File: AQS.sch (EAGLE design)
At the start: 44 parts, among them IC1 BME680, IC3 CP2102N-A01-GQFN24, IC4 ESPWROOM32, J1 ESP-PROG-2X3-1.27-SHROUDED, J2 M02X5-1.27-S, J3 USB-C-16P-16P, Q1 MMDT3904, Q2 2N7002

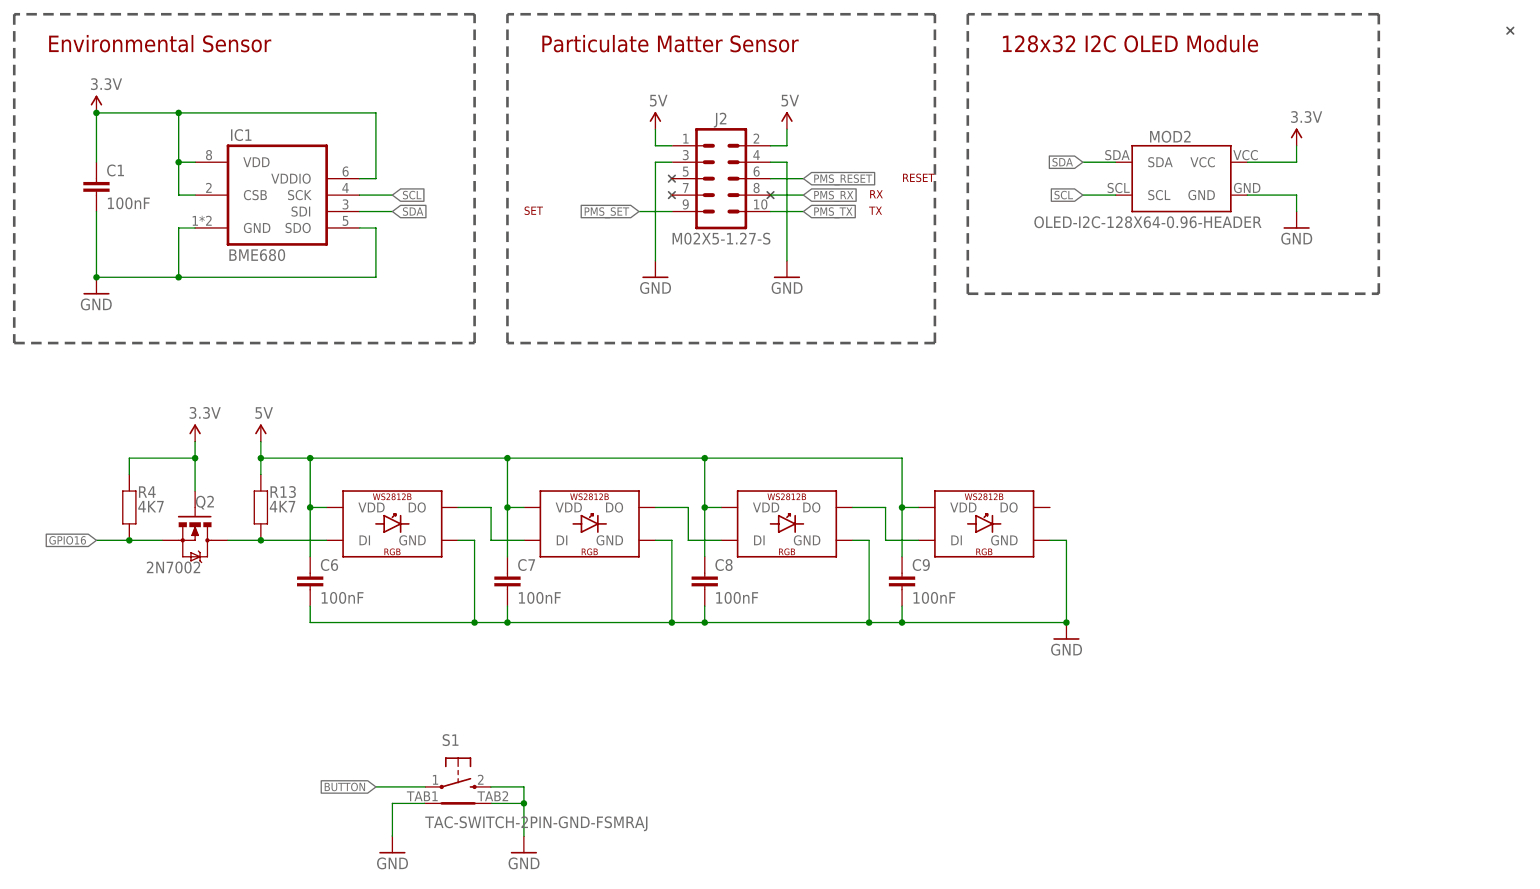
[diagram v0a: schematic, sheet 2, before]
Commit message: Major update to use 240x240 SPI LCD
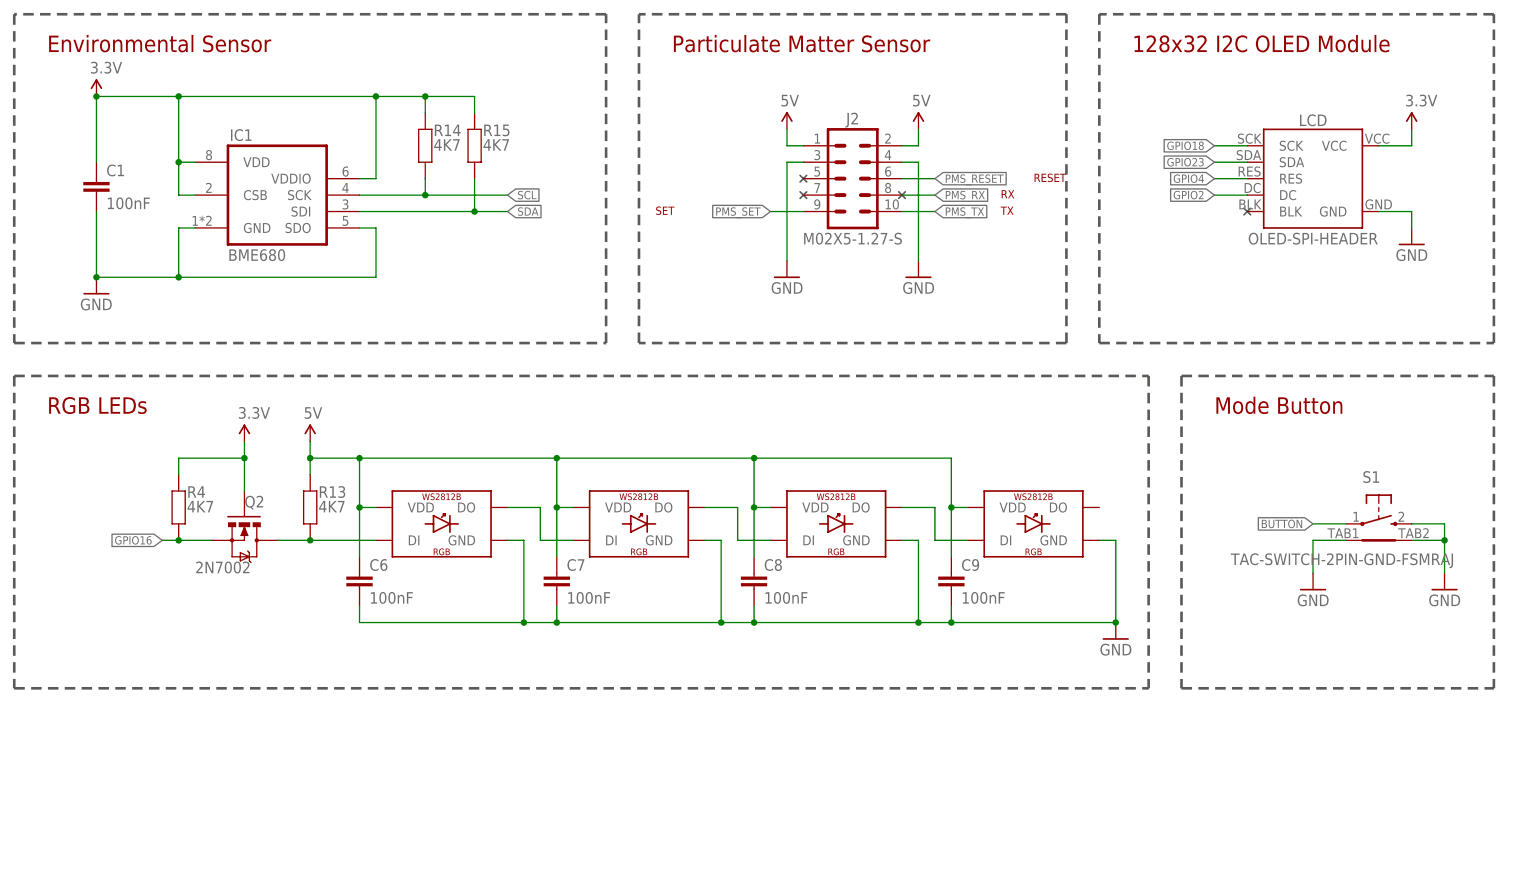
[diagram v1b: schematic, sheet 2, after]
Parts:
- removed MOD2: OLED-I2C-128X64-0.96-HEADER, SuperHouse-Displays:OLED-I2C-128X64-0.96-HEADER
- added LCD: OLED-SPI-HEADER, SuperHouse-Displays:OLED-SPI-HEADER
- added R14, R15: 4K7, SuperHouse-DiscreteSemi:RESISTOR0603
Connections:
- new net GPIO15: IC4.IO15
- new net GPIO18: IC4.IO18, LCD.SCK
- new net GPIO19: IC4.IO19
- new net GPIO2: IC4.IO2, LCD.DC
- new net GPIO23: IC4.IO23, LCD.SDA
- new net GPIO4: IC4.IO4, LCD.RES
- net 3.3V: now also LCD.VCC, R14.2, R15.2; no longer MOD2.VCC
- net GND: now also LCD.GND; no longer MOD2.GND
- net SCL: now also R14.1; no longer MOD2.SCL
- net SDA: now also R15.1; no longer MOD2.SDA
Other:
- note added: "Enable INPUT_PULLUP on IO35: button is active low"
- note added: "GPIO2: TFT_DC GPIO4: TFT_RST GPIO14: SET for PMS7003 GPIO15: TFT_CS GPIO16: WS2812B GPIO18: TFT_SCLK GPIO19: TFT_MISO GPIO23: TFT_MOSI GPIO25: SDA GPIO26: SCL GPIO34: Rx from PMS7003 Tx GPIO35: Button Firmware: https://github.com/openairproject/sensor-esp32"
- note added: "I2C Address: 0x77: BME680"
- note added: "Mode Button"
- note added: "RGB LEDs"
- note removed: "Assign pins Add ESPRog header and remove RST button? Remove power LED? Hide parts in bottom tab"
- note removed: "Enable INPUT_PULLUP on IO25, 26, 27: alert lines are active low"
- note removed: "GPIO14: SET for PMS7003 GPIO16: WS2812B GPIO25: SDA GPIO26: SCL GPIO34: Rx from PMS7003 Tx GPIO35: Button Firmware: https://github.com/openairproject/sensor-esp32"
- note removed: "I2C Addresses: 0x40: PCA9685 0x41: INA233 channel 1 0x42: INA233 channel 2 0x43: INA233 channel 3 0x66: ? 0x70: ? 0x77: BME280"
- note removed: "Power"
- moved on the sheet: C2, C3, C4, C5, C6, C7, C8, C9, IC4, J2, LED1, Q2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

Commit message: Moved mode button to GPIO0
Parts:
- removed S1: TAC-SWITCH-2PIN-GND-FSMRAJ, SuperHouse-Switches:TAC-SWITCH-2PIN-GND-FSMRAJ
- added S3: (no value), SuperHouse-Switches:TAC_SWITCH-PTH-4.5
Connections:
- removed net BUTTON: IC4.IO35, S1.1
- net GND: now also S3.3, S3.4; no longer S1.2, S1.TAB1, S1.TAB2
- net GPIO0: now also S3.1, S3.2
- net PMS_RESET: now also IC4.IO27
- net PMS_RX: now also IC4.IO12
- net PMS_TX: now also IC4.IO17; no longer IC4.IO34
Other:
- note added: "GPIO0: Button GPIO2: TFT_DC GPIO4: TFT_RST GPIO14: PMS7003 SET GPIO15: TFT_CS GPIO16: WS2812B GPIO18: TFT_SCLK GPIO19: TFT_MISO GPIO23: TFT_MOSI GPIO25: SDA GPIO26: SCL GPIO27: PMS7003 RESET GPIO31: Tx to PMS7003 Rx GPIO34: Rx from PMS7003 Tx Firmware: https://github.com/openairproject/sensor-esp32"
- note removed: "GPIO2: TFT_DC GPIO4: TFT_RST GPIO14: SET for PMS7003 GPIO15: TFT_CS GPIO16: WS2812B GPIO18: TFT_SCLK GPIO19: TFT_MISO GPIO23: TFT_MOSI GPIO25: SDA GPIO26: SCL GPIO34: Rx from PMS7003 Tx GPIO35: Button Firmware: https://github.com/openairproject/sensor-esp32"
- note removed: "PMS SET"
- moved on the sheet: F1

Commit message: Replaced CP2102N with CH340G; removed 2 LEDs; reworked routing; moved button
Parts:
- removed C7, C9: 100nF, SuperHouse-DiscreteSemi:CAP0603
- removed IC3: CP2102N-A01-GQFN24, SuperHouse-ICs:CP2104
- removed LED3, LED5: WS2812B5050, SuperHouse-LEDs:WS2812B5050
- removed LED8: GREEN, SuperHouse-LEDs:LED0603
- removed LED9: YELLOW, SuperHouse-LEDs:LED0603
- removed R2, R3: 1K, SuperHouse-DiscreteSemi:RESISTOR0603
- removed R8: 22.1K, SuperHouse-DiscreteSemi:RESISTOR0603
- removed R9: 47.5K, SuperHouse-DiscreteSemi:RESISTOR0603
- added C10, C11: 22pF, SuperHouse-DiscreteSemi:CAP0603
- added C12: 100nF, SuperHouse-DiscreteSemi:CAP0603
- added IC2: CH340G, SuperHouse-ICs:CH340GSMD
- added U$1: 16MHz, SuperHouse-Oscillators:CRYSTAL-GND3X2
- C2: value 4.7uF -> 10uF
- C3: value 1uF -> 10uF
- S1: value (none) -> MODE
- renumbered S3 to S1
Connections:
- removed net ESP_RX: IC3.TXD, IC4.RXD0, J1.ESP_RX
- removed net ESP_TX: IC3.RXD, IC4.TXD0, J1.ESP_TX
- removed net GPIO15: IC4.IO15
- removed net GPIO19: IC4.IO19
- removed net N$13: LED4.DO, LED5.DI
- removed net N$5: LED9.C, R3.2
- removed net N$6: IC3.VBUS, R8.1, R9.2
- removed net N$9: LED2.DO, LED3.DI
- new net RXD0: IC2.TXD, IC4.RXD0, J1.ESP_RX
- new net TXD0: IC2.RXD, IC4.TXD0, J1.ESP_TX
- net 3.3V: now also C12.1, IC2.V3, IC2.VCC; no longer IC3.REGIN, IC3.VDD, IC3.VIO, LED8.A, LED9.A
- net 5V: no longer C7.1, C9.1, LED3.VDD, LED5.VDD, R8.2
- net D+: now also IC2.UD+; no longer IC3.D+
- net D-: now also IC2.UD-; no longer IC3.D-
- net DTR: now also IC2.!DTR; no longer IC3.DTR
- net GND: now also C10.2, C11.2, C12.2, IC2.GND, U$1.GND, U$1.GND2; no longer C7.2, C9.2, IC3.GND, IC3.GND_PAD, LED3.GND, LED5.GND, R9.1
- net N$12: now also LED2.DO; no longer LED3.DO
- net N$2: now also C10.1, IC2.XO, U$1.XTL2; no longer IC3.GPIO_0, R3.1
- net N$3: now also C11.1, IC2.XI, U$1.XTL1; no longer IC3.GPIO_1, R2.1
- net N$4: now also IC4.IO34; no longer LED8.C, R2.2
- net RTS: now also IC2.!RTS; no longer IC3.RTS
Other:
- note added: "ESP-Prog Header"
- note added: "GPIO0: Button GPIO2: TFT_DC GPIO4: TFT_RST GPIO12: Tx to PMS7003 Rx GPIO14: PMS7003 SET GPIO15: TFT_CS GPIO16: WS2812B GPIO17: Rx from PMS7003 Tx GPIO18: TFT_SCLK GPIO19: TFT_MISO GPIO23: TFT_MOSI GPIO25: SDA GPIO26: SCL GPIO27: PMS7003 RESET Firmware: https://github.com/openairproject/sensor-esp32"
- note added: "V2.0 (2020-03-24)"
- note removed: "GPIO0: Button GPIO2: TFT_DC GPIO4: TFT_RST GPIO14: PMS7003 SET GPIO15: TFT_CS GPIO16: WS2812B GPIO18: TFT_SCLK GPIO19: TFT_MISO GPIO23: TFT_MOSI GPIO25: SDA GPIO26: SCL GPIO27: PMS7003 RESET GPIO31: Tx to PMS7003 Rx GPIO34: Rx from PMS7003 Tx Firmware: https://github.com/openairproject/sensor-esp32"
- note removed: "RESET"
- note removed: "RX"
- note removed: "SET"
- note removed: "TX"
- note removed: "V1.0 (2020-02-04)"
- note removed: "WS2812B"
- moved on the sheet: C4, C5, C8, IC4, J1, Q1Q1, Q1Q2, R11, R12, R5, R7, S2

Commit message: Replaced programming header
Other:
- moved on the sheet: C10, C11, C12, C4, C5, F1, IC2, IC4, J1, J3, Q1Q1, Q1Q2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

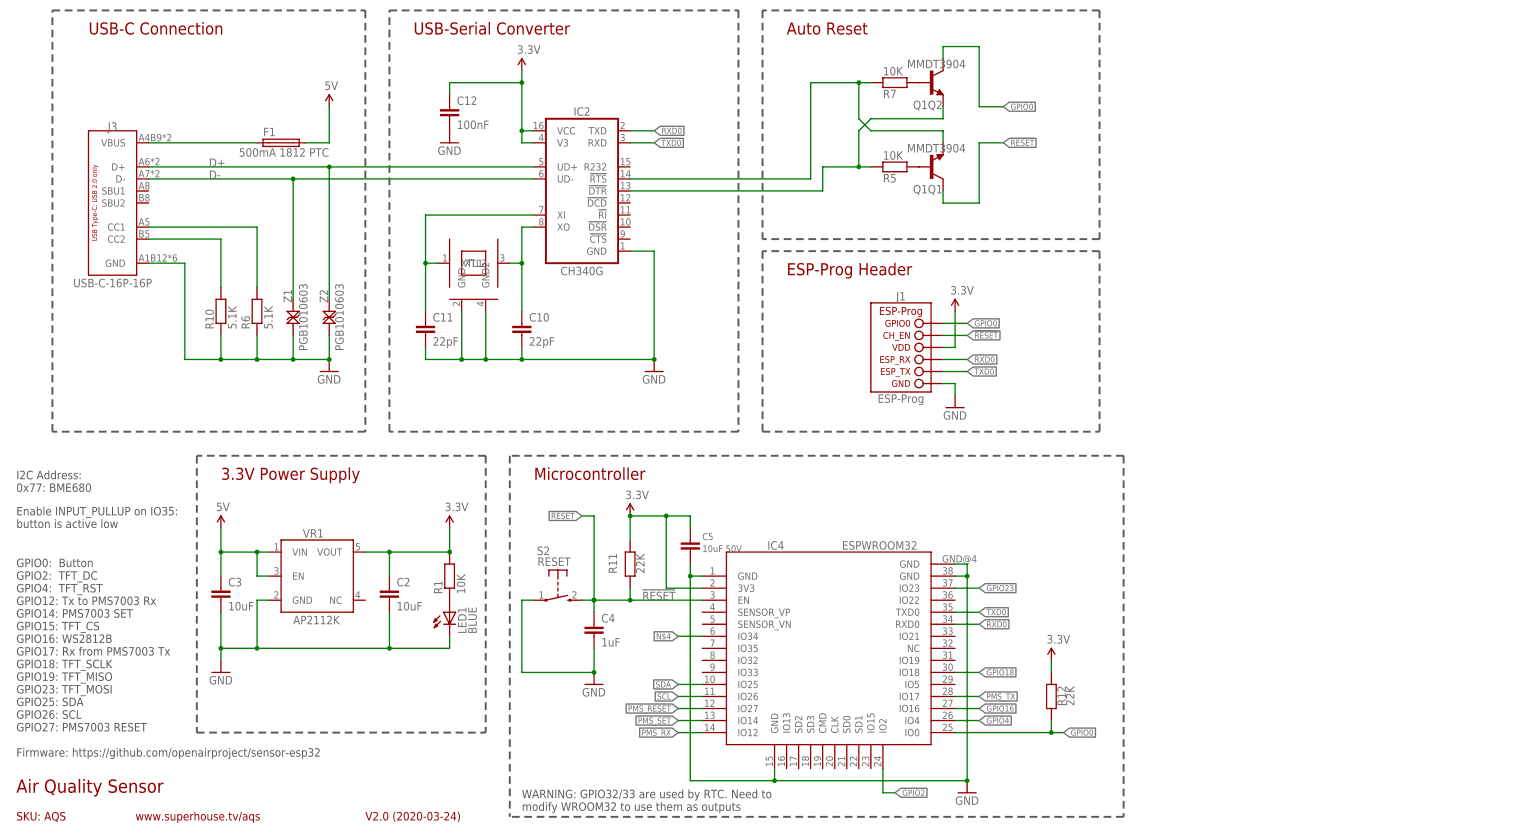
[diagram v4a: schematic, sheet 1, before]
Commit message: Routing for CP2102N
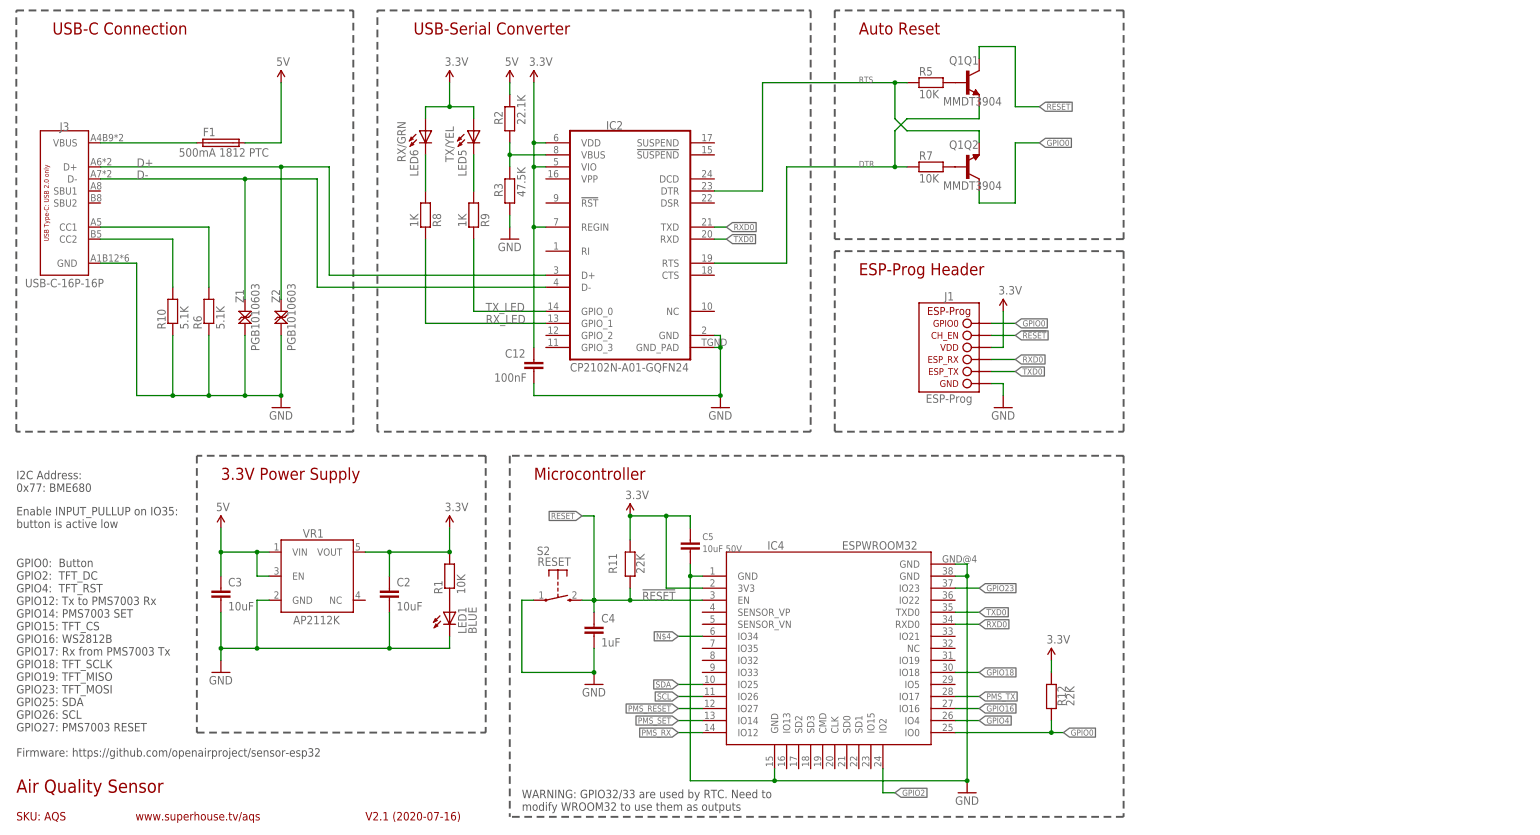
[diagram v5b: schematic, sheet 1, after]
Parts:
- removed C10, C11: 22pF, SuperHouse-DiscreteSemi:CAP0603
- removed U$1: 16MHz, SuperHouse-Oscillators:CRYSTAL-GND3X2
- added LED5: TX/YEL, SuperHouse-LEDs:LED0603
- added LED6: RX/GRN, SuperHouse-LEDs:LED0603
- added R2: 22.1K, SuperHouse-DiscreteSemi:RESISTOR0603
- added R3: 47.5K, SuperHouse-DiscreteSemi:RESISTOR0603
- added R8, R9: 1K, SuperHouse-DiscreteSemi:RESISTOR0603
- IC2: value CH340G -> CP2102N-A01-GQFN24; device SuperHouse-ICs:CH340GSMD -> SuperHouse-ICs:CP2104
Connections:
- removed net N$3: C11.1, IC2.XI, U$1.XTL1
- new net N$13: LED5.C, R9.2
- new net N$39: IC2.VBUS, R2.1, R3.2
- new net RX_LED: IC2.GPIO_1, R8.1
- new net TX_LED: IC2.GPIO_0, R9.1
- net 3.3V: now also IC2.REGIN, IC2.VDD, IC2.VIO, LED5.A, LED6.A; no longer IC2.V3, IC2.VCC
- net 5V: now also R2.2
- net D+: now also IC2.D+; no longer IC2.UD+
- net D-: now also IC2.D-; no longer IC2.UD-
- net DTR: now also IC2.DTR; no longer IC2.!DTR
- net GND: now also IC2.GND_PAD, R3.1; no longer C10.2, C11.2, U$1.GND, U$1.GND2
- net N$2: now also LED6.C, R8.2; no longer C10.1, IC2.XO, U$1.XTL2
- net RTS: now also IC2.RTS; no longer IC2.!RTS
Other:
- note added: "V2.1 (2020-07-16)"
- note removed: "V2.0 (2020-03-24)"
- moved on the sheet: C12, F1, J1, J3, Q1Q1, Q1Q2, R10, R5, R6, R7, Z1, Z2
